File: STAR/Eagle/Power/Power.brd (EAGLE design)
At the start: 66 x 44.5 mm, 24 parts, among them J1 J30J-9J30, T1 750311838, U1 LT8300, U2 LT8330

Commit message: Power Board
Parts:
- removed D4: PMEG6010CEJ, AR_diode:SOD323
- removed T1: 750311838, AR_transformer:750311838
- added C10, C11, C12: .18 uF, resistor:C0603
- added C13, C14, C15: 10 uF, resistor:C0603
- added C16, C18, C20, C22, C24: KTJ500B476M76BFT00, Filtering:STACKED
- added C17, C19, C21, C23, C25: 1nF, resistor:C0603
- added C8, C9: .1 uF, resistor:C0603
- added L2: 5.5u, Filtering:1050
- added L3: 3.7u, Power:1365
- added L4, L5, L6, L7, L8: 744029000068, Filtering:2813
- added R9: 13.3k, resistor:R0603
- added U$1, U$2: DFT7160-105B, Filtering:DFT7160
- added U3: LMR16020, HASP:SO8
- C1: value 22uF -> 10 uF; device AR_passives:3025 -> resistor:C1210
- C2: value 1uF -> 10 uF; device AR_passives:0603 -> resistor:C1210
- C3: value (none) -> 10 uF
- C4: value 10uF -> 2.2 uF; device AR_passives:2J-LEAD -> resistor:C1210
- C5: value 1uF -> 2.2 uF; device AR_passives:0603 -> resistor:C1210
- C6: value 4.7pF -> 2.2 uF; device AR_passives:0603 -> resistor:C1210
- C7: value 1uF -> .1 uF; device AR_passives:0603 -> resistor:C0603
- D1: value MMSZ5266BT1G -> DO-214AC; device AR_diode:SOD123 -> HASP:DO-214AC
- D2: value BAV20W -> DO-214AC; device AR_diode:SOD323 -> HASP:DO-214AC
- D3: value SBR0560S1 -> DO-214AC; device AR_diode:SOD123 -> HASP:DO-214AC
- J1: value J30J-9J30 -> J30J-25; device CM_J30J:ZKN-9-J30 -> CM_J30J:ZKN-25
- L1: value 10uH -> 9.7u; device AR_passives:PQ2614 -> Power:7050
- R1: value 47k -> 23.2k; device resistor:R2512 -> resistor:R0603
- R2: value 407k -> 23.2k
- R3: value 1k -> 23.2k
- R4: value 3k -> 199.5k; device resistor:R2512 -> resistor:R0603
- R5: value 1.5k -> 13.3k; device resistor:R2512 -> resistor:R0603
- R6: value 1M -> 75.4k
- R7: value 33k -> 13.3k
- R8: value 52.6 -> 45.2k
- U1: value LT8300 -> LMR16020; device AR_IC:SOT23-5 -> HASP:SO8
- U2: value LT8330 -> LMR16020; device AR_IC:8-DFN -> HASP:SO8
- moved C7 32.3 mm to (21.5, 32.6), turned to 180 degrees
- moved C3 24.4 mm to (5.46, 9.53), turned to 180 degrees
- moved R2 24.4 mm to (15.4, -4.64), turned to 180 degrees
- moved C1 23.0 mm to (15.2, 27.4), turned to 0 degrees
- moved R4 22.2 mm to (26.3, 23.9), turned to 270 degrees
- moved C2 21.1 mm to (11.6, -2.92), turned to 270 degrees
- moved R5 20.2 mm to (24.0, 23.9), turned to 90 degrees
- moved C5 19.6 mm to (7.11, 6.22)
- moved R7 19.1 mm to (18.8, -4.69), turned to 0 degrees
- moved R1 18.9 mm to (19.6, 23.9)
- moved D3 18.5 mm to (12.2, 8.89)
- moved D2 18.2 mm to (24.8, 8.06), turned to 0 degrees
- moved C6 17.8 mm to (11.9, 2.41), turned to 270 degrees
- moved J1 16.1 mm to (-1.27, 22.9), turned to 90 degrees
- moved L1 14.7 mm to (36.3, 27.8), turned to 90 degrees
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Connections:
- removed net +20V: C3.1, C5.1, D3.P$2, L1.P$2, U2.P$6, U2.P$8
- removed net +50V: C4.P$1, C6.1, D4.P$2, J1.1, J1.2, R1.2, R5.2, R6.2
- removed net N$11: R7.1, R8.2
- removed net VCC: C1.P$1, C2.1, D1.P$1, J1.4, T1.P$3, U1.1, U1.5
- removed net V_DIVIDE: J1.5, R1.1, R4.2
- new net +12V: C10.1, C13.1, L1.P$2, L8.P$1, R4.2
- new net +3V3: C12.1, C15.1, L3.P$2, L6.P$1, R8.2
- new net +5V: C11.1, C14.1, L2.P$2, L5.P$1, R6.2
- new net 12V_FILT: C24.P$1, C25.1, J1.3, L8.P$2
- new net 3V3_FILT: C20.P$1, C21.1, J1.1, L6.P$2
- new net 5V_FILT: C18.P$1, C19.1, J1.16, J1.18, J1.2, J1.8, L5.P$2
- new net D: J1.10
- new net ER: J1.12
- new net F: J1.6
- new net GSE_FILT: C16.P$1, C17.1, C2.1, C3.1, C5.1, C6.1, L4.P$2, U2.P$2, U2.P$3, U3.P$2, U3.P$3
- new net GSE_GND: C11.2, C12.2, C14.2, C15.2, C16.P$2, C17.2, C18.P$2, C19.2, C2.2, C20.P$2, C21.2, C3.2, C5.2, C6.2, D2.P$1, D3.P$1, J1.14, J1.17, J1.19, J1.20, J1.21, J1.22, R2.1, R3.1, R7.1, R9.1, U2.P$7, U2.PAD, U3.P$7, U3.PAD
- new net GSE_UFILT: J1.15, U$1.P$1, U$1.P$2
- new net I: J1.4
- new net N$14: C7.1, D1.P$2, L1.P$1, U1.P$8
- new net N$27: R4.1, R5.2, U1.P$5
- new net N$28: L4.P$1, U$1.P$3, U$1.P$4
- new net N$29: L7.P$1, U$2.P$3, U$2.P$4
- new net N$44: J1.25
- new net N$45: J1.24
- new net N$46: J1.23
- new net N$8: R8.1, R9.2, U3.P$5
- new net Q: J1.7
- new net T: J1.5
- new net TE_FILT: C1.1, C22.P$1, C23.1, C4.1, L7.P$2, U1.P$2, U1.P$3
- new net TE_UFILT: J1.13, U$2.P$1, U$2.P$2
- net GND: now also C1.2, C10.2, C13.2, C22.P$2, C23.2, C24.P$2, C25.2, C4.2, D1.P$1, J1.11, J1.9, R1.1, U1.P$7, U1.PAD; no longer C1.P$2, C2.2, C3.2, C4.P$2, C5.2, C7.2, J1.6, J1.7, R4.1, R8.1, T1.P$7, U1.2, U2.P$5, U2.P$9
- net N$1: now also R3.2, U3.P$4; no longer D1.P$2, D2.P$2
- net N$10: now also C7.2, U1.P$1; no longer J1.9
- net N$2: now also C9.1, D3.P$2, L3.P$1, U3.P$8; no longer R2.1, U1.3
- net N$3: now also U2.P$4; no longer R3.1
- net N$4: now also C8.2, U2.P$1; no longer D2.P$1, R3.2, T1.P$4, U1.4
- net N$5: now also C8.1, D2.P$2, L2.P$1, U2.P$8; no longer D3.P$1, T1.P$6
- net N$6: now also C9.2, U3.P$1; no longer C7.1, U2.P$7
- net N$7: now also R1.2, U1.P$4; no longer D4.P$1, L1.P$3, U2.P$3, U2.P$4
- net N$9: now also U2.P$5; no longer C6.2, U2.P$1
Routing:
- net 5V_FILT: track 0.00 -> 61.2 mm, vias 0 -> 1
- net +50V: track 57.6 -> 0.00 mm
- net 12V_FILT: track 0.00 -> 57.0 mm, vias 0 -> 1
- net GND: track 55.8 -> 3.14 mm, vias 14 -> 6
- net N$7: track 48.8 -> 2.37 mm, vias 3 -> 0
- net 3V3_FILT: track 0.00 -> 45.6 mm
- net GSE_FILT: track 0.00 -> 44.1 mm, vias 0 -> 2
- net +20V: track 43.6 -> 0.00 mm
- net VCC: track 43.1 -> 0.00 mm
- net +12V: track 0.00 -> 42.8 mm, vias 0 -> 3
- net N$2: track 3.21 -> 37.4 mm, vias 0 -> 2
- net GSE_GND: track 0.00 -> 34.1 mm, vias 0 -> 14
- net N$14: track 0.00 -> 33.0 mm, vias 0 -> 2
- net N$9: track 36.7 -> 4.11 mm, vias 4 -> 0
- net TE_FILT: track 0.00 -> 24.9 mm
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- added copper zone on layer 16, net +12V
- added copper zone on layer 16, net +3V3
- added copper zone on layer 16, net +5V
- added copper zone on layer 16, net 5V_FILT
- added copper zone on layer 1, net GSE_GND
- added copper zone on layer 16, net GSE_UFILT
- added copper zone on layer 16, net TE_UFILT
- removed copper zone on layer 16, net GND
- removed copper zone on layer 1, net N$7
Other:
- board size 66 x 44.5 mm -> 58.2 x 40.4 mm

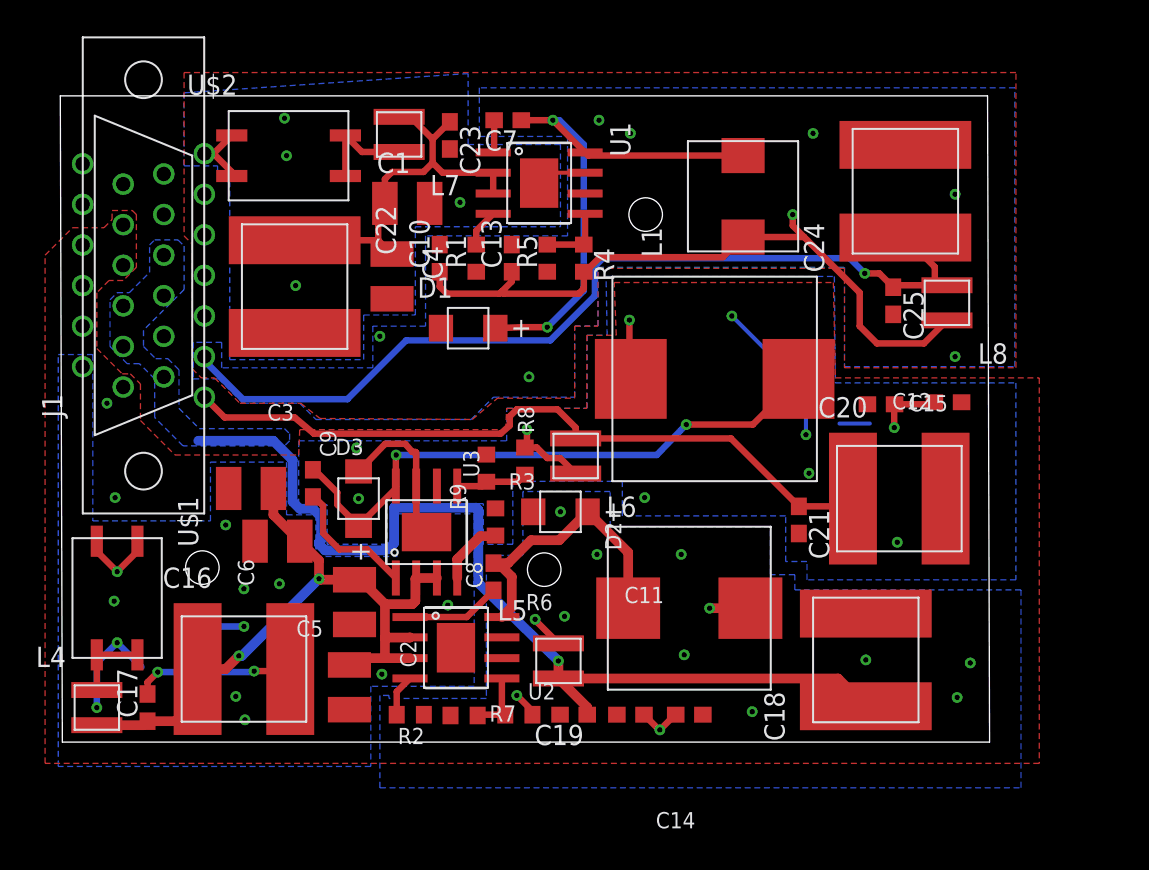
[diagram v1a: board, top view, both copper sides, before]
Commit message: new filtering caps for power board
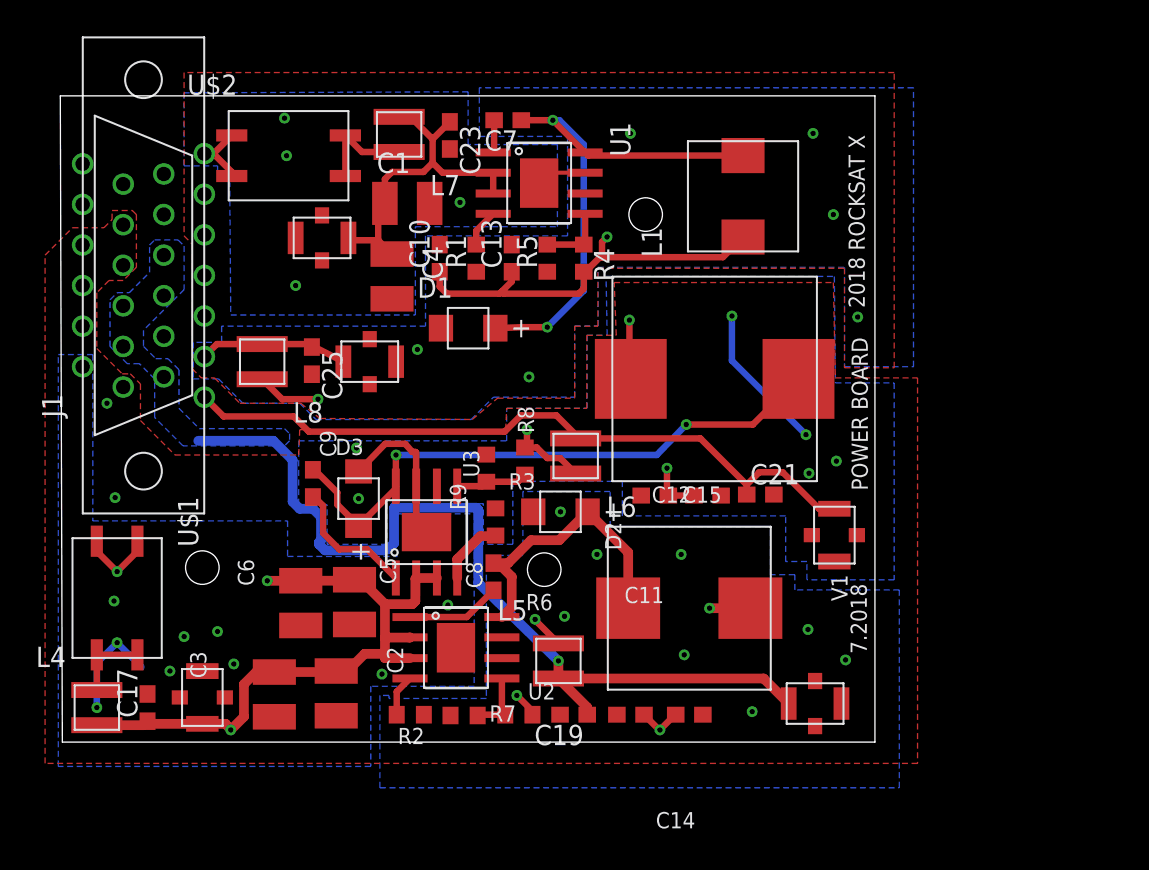
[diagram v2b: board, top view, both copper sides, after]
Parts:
- removed C16, C18, C20, C22, C24: KTJ500B476M76BFT00, Filtering:STACKED
- added U$3, U$4, U$5, U$6, U$7: 1410J0500404MXTE03, Filtering:1410
- moved L8 43.0 mm to (6.16, 17.5)
- moved C25 36.6 mm to (9.27, 17.5)
- moved C12 16.1 mm to (34.0, 9.08)
- moved C15 15.3 mm to (30.7, 9.08)
- moved C3 13.0 mm to (6.92, -3.37), turned to 270 degrees
- moved C5 4.14 mm to (8.57, 2.35), turned to 270 degrees
- moved C21 2.89 mm to (37.3, 9.14), turned to 0 degrees
- moved C2 0.91 mm to (10.8, -3.30)
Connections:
- net 12V_FILT: now also U$7.P$3; no longer C24.P$1
- net 3V3_FILT: now also U$5.P$3; no longer C20.P$1
- net 5V_FILT: now also U$4.P$3; no longer C18.P$1
- net GND: now also U$6.P$2, U$6.P$4, U$6.P$5, U$7.P$2, U$7.P$4, U$7.P$5; no longer C22.P$2, C24.P$2
- net GSE_FILT: now also U$3.P$3; no longer C16.P$1
- net GSE_GND: now also U$3.P$2, U$3.P$4, U$3.P$5, U$4.P$2, U$4.P$4, U$4.P$5, U$5.P$2, U$5.P$4, U$5.P$5; no longer C16.P$2, C18.P$2, C20.P$2
- net TE_FILT: now also U$6.P$3; no longer C22.P$1
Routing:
- net 12V_FILT: track 57.0 -> 9.32 mm, vias 1 -> 0
- net GSE_GND: track 34.1 -> 19.2 mm, vias 14 -> 11
- net +12V: track 42.8 -> 29.2 mm
- net 5V_FILT: track 61.2 -> 56.3 mm
- net TE_FILT: track 24.9 -> 21.6 mm
- net GSE_FILT: track 44.1 -> 40.8 mm
- net GSE_UFILT: track 14.4 -> 11.6 mm, vias 9 -> 7
- net 3V3_FILT: track 45.6 -> 44.6 mm
- net +3V3: track 12.8 -> 12.1 mm, vias 7 -> 6
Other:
- board size 58.2 x 40.4 mm -> 51 x 40.4 mm
- board text added: "2018 ROCKSAT X"
- board text added: "7.2018"
- board text added: "POWER BOARD"
- board text added: "V1"

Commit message: Fixed the three terminal capacitor routing (five capacitors).
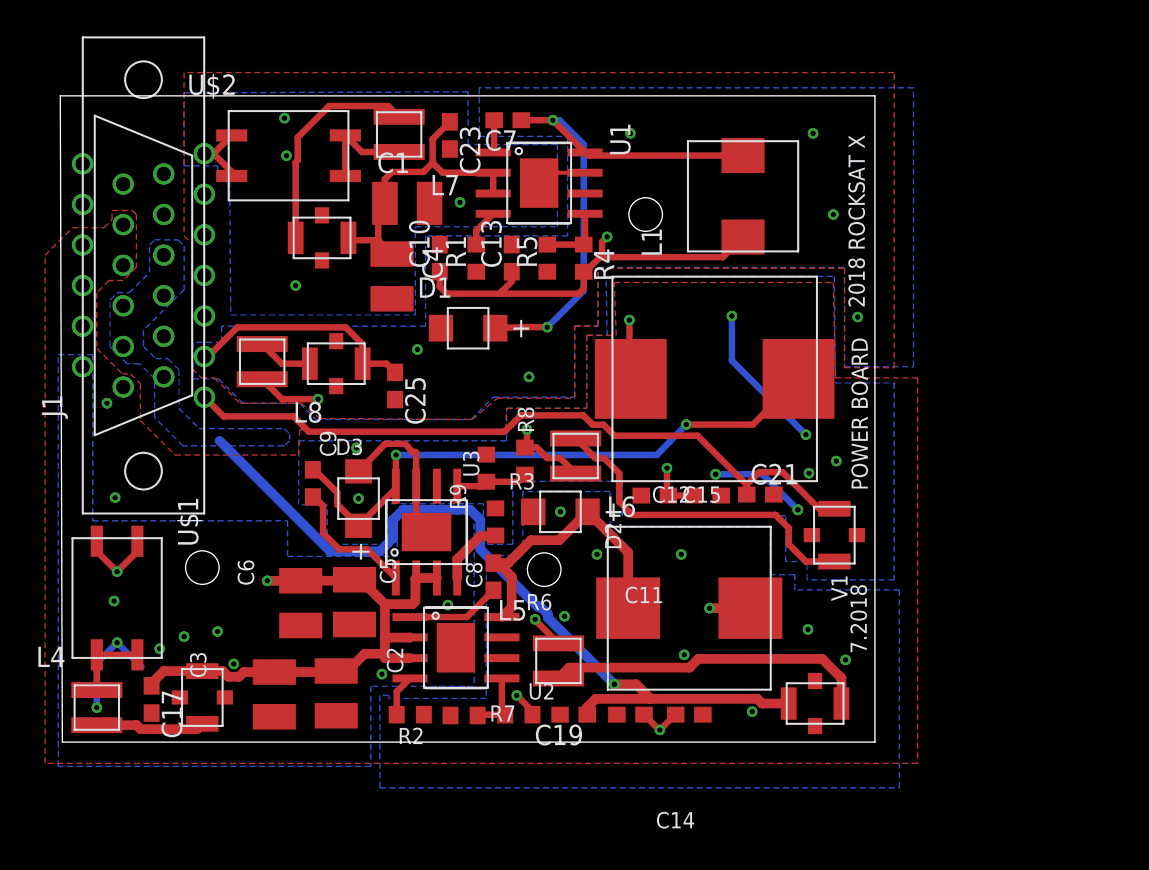
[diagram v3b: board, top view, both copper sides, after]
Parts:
- moved C25 5.44 mm to (14.5, 15.9)
- moved U$7 2.10 mm to (10.8, 17.3), turned to 180 degrees
- moved C17 0.57 mm to (-0.76, -3.68), turned to 270 degrees
- turned U$4 to 180 degrees
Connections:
- removed net D: J1.10
- removed net ER: J1.12
- removed net F: J1.6
- removed net I: J1.4
- removed net N$44: J1.25
- removed net N$45: J1.24
- removed net N$46: J1.23
- removed net Q: J1.7
- removed net T: J1.5
- new net N$31: L4.P$2, U$3.P$3
- new net N$32: L5.P$2, U$4.P$3
- new net N$33: L6.P$2, U$5.P$2
- new net N$34: L7.P$2, U$6.P$2
- new net N$35: L8.P$2, U$7.P$2
- net 12V_FILT: no longer L8.P$2
- net 3V3_FILT: no longer L6.P$2
- net 5V_FILT: now also U$4.P$2; no longer L5.P$2, U$4.P$3
- net GND: no longer U$6.P$2, U$7.P$2
- net GSE_FILT: now also U$3.P$2; no longer L4.P$2, U$3.P$3
- net GSE_GND: no longer U$3.P$2, U$4.P$2, U$4.P$4, U$4.P$5, U$5.P$2
- net TE_FILT: no longer L7.P$2
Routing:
- net N$33: track 0.00 -> 21.0 mm
- net N$32: track 0.00 -> 20.3 mm
- net N$34: track 0.00 -> 13.8 mm
- net N$31: track 0.00 -> 6.85 mm
- net GSE_GND: track 19.2 -> 25.2 mm, vias 11 -> 13
- net GSE_FILT: track 40.8 -> 35.1 mm, vias 2 -> 1
- net 12V_FILT: track 9.32 -> 14.6 mm
- net 5V_FILT: track 56.3 -> 51.1 mm
- net N$35: track 0.00 -> 3.49 mm
- net TE_FILT: track 21.6 -> 18.9 mm

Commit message: fixed choke routing on power board
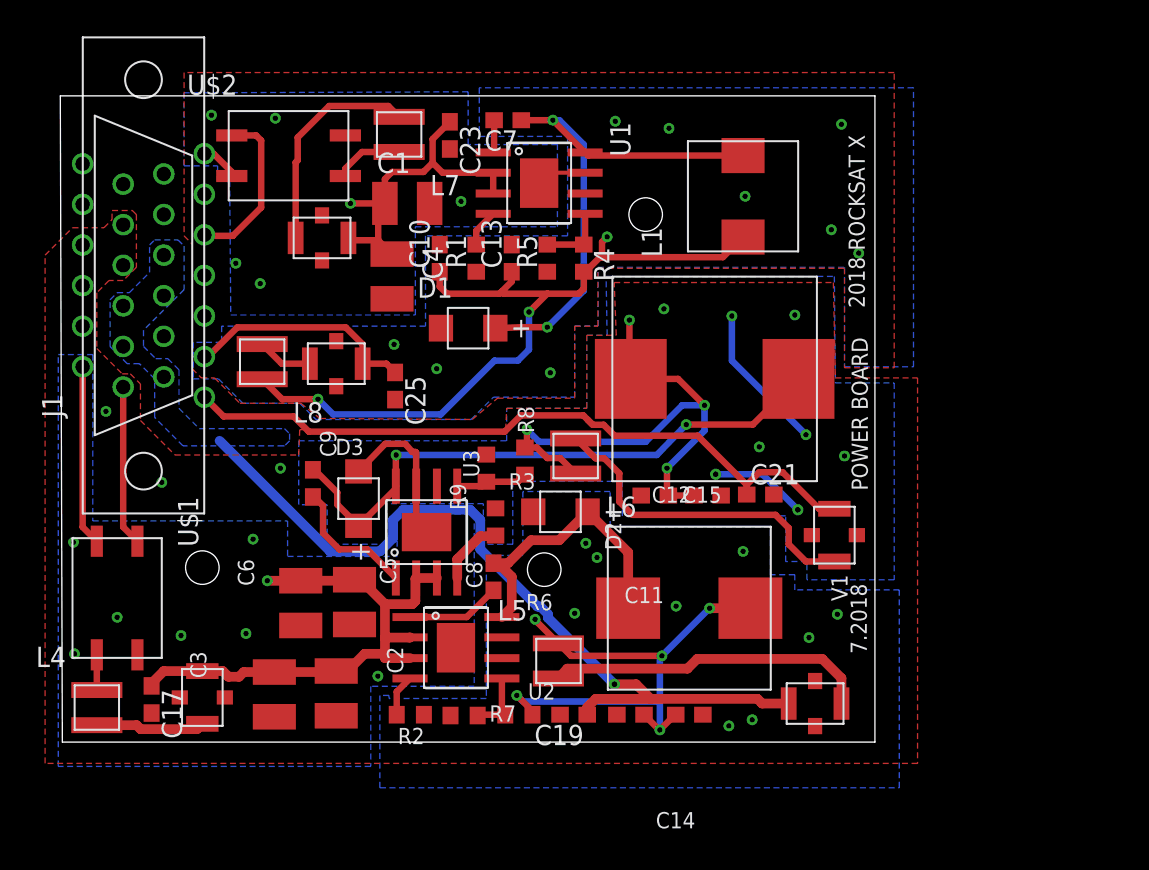
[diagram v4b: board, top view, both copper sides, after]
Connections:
- removed net GSE_GND: C11.2, C12.2, C14.2, C15.2, C17.2, C19.2, C2.2, C21.2, C3.2, C5.2, C6.2, D2.P$1, D3.P$1, J1.14, J1.17, J1.19, J1.20, J1.21, J1.22, R2.1, R3.1, R7.1, R9.1, U$3.P$4, U$3.P$5, U$5.P$4, U$5.P$5, U2.P$7, U2.PAD, U3.P$7, U3.PAD
- removed net TE_UFILT: J1.13, U$2.P$1, U$2.P$2
- new net +3V3_FILT: C11.2, C12.2, C14.2, C15.2, C17.2, C19.2, C2.2, C21.2, C3.2, C5.2, C6.2, D2.P$1, D3.P$1, J1.17, J1.19, J1.20, J1.21, J1.22, R2.1, R3.1, R7.1, R9.1, U$1.P$4, U$3.P$4, U$3.P$5, U$5.P$4, U$5.P$5, U2.P$7, U2.PAD, U3.P$7, U3.PAD
- new net GND_IN: J1.9, U$2.P$1
- new net GSE_GND_IN: J1.14, U$1.P$1
- new net N$37: J1.6
- new net N$38: J1.5
- new net N$39: J1.4
- new net TEUFILT: J1.13, U$2.P$2
- net GND: now also J1.7, U$2.P$4; no longer J1.11, J1.9
- net GSE_UFILT: no longer U$1.P$1
- net N$28: no longer U$1.P$4
- net N$29: no longer U$2.P$4
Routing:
- net GSE_GND: track 25.2 -> 0.00 mm, vias 13 -> 0
- net +3V3_FILT: track 0.00 -> 25.2 mm, vias 0 -> 19
- net +5V: track 9.04 -> 33.9 mm, vias 9 -> 5
- net +3V3: track 12.1 -> 34.7 mm, vias 6 -> 4
- net +12V: track 29.2 -> 48.5 mm
- net GND_IN: track 0.00 -> 10.5 mm
- net GSE_GND_IN: track 0.00 -> 10.0 mm
- net TE_UFILT: track 4.06 -> 0.00 mm, vias 3 -> 0
- net N$28: track 4.74 -> 2.20 mm
- net TEUFILT: track 0.00 -> 2.44 mm
- net TE_FILT: track 18.9 -> 21.1 mm, vias 0 -> 4
- net N$29: track 6.33 -> 4.26 mm
- net GSE_UFILT: track 11.6 -> 11.9 mm, vias 7 -> 0
- net GSE_FILT: vias 1 -> 4
- net GND: vias 6 -> 5
- added copper zone on layer 16, net +12V_FILT
- added copper zone on layer 1, net +3V3_FILT
- added copper zone on layer 16, net +3V3_FILT
- added copper zone on layer 16, net +5V_FILT
- added copper zone on layer 16, net GSE_FILT
- added copper zone on layer 16, net TE_FILT
- removed copper zone on layer 16, net +12V
- removed copper zone on layer 16, net +3V3
- removed copper zone on layer 16, net +5V
- removed copper zone on layer 1, net GSE_GND
- removed copper zone on layer 16, net GSE_UFILT
- removed copper zone on layer 16, net TE_UFILT

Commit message: I think I fixed all of the GSE_GND being '+3V3_FILT' but I don't know how that happened in the first place
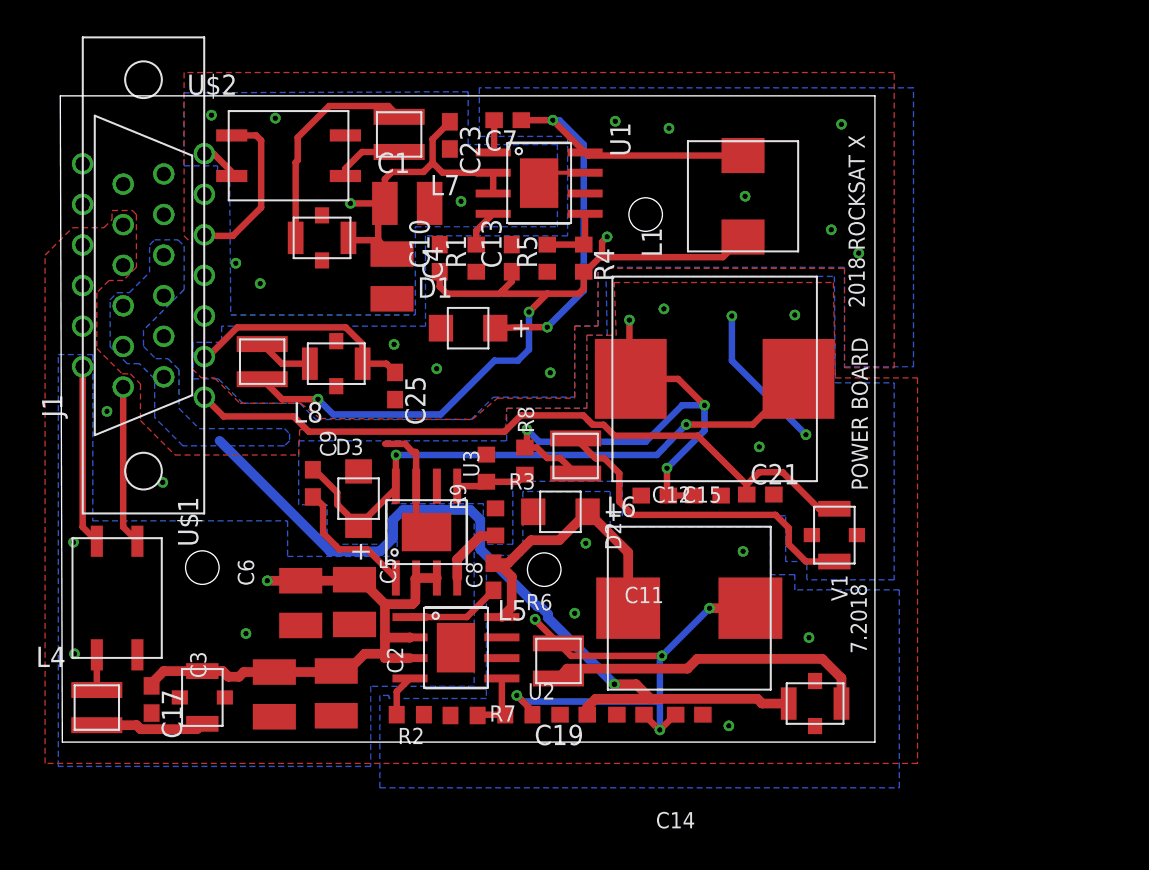
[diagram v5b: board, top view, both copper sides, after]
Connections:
- net +3V3_FILT renamed GSE_GND
- net N$37 renamed E
- net N$38 renamed F
- net N$39 renamed D
- net TEUFILT renamed TE_UFILT
- new net EW: J1.12
- new net G: J1.10
- new net N$40: J1.11
- new net N$42: J1.25
- new net N$43: J1.24
- new net N$44: J1.23
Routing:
- net GSE_GND: track 25.2 -> 16.8 mm, vias 19 -> 7
